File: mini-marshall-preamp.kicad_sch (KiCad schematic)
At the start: 46 parts, among them J1 LO, J2 HI, J3 OUT, J4 6V3, J5 370V GND, J6 370V, J7 6V3 GND, J8 6V3, J9 6V3 GND, U1 6N2P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

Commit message: Nice layout
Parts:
- J1: footprint Connector_Wire:SolderWire-1sqmm_1x03_P7.8mm_D1.4mm_OD3.9mm -> Connector_Wire:SolderWire-1sqmm_1x04_P7.8mm_D1.4mm_OD3.9mm
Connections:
- net anode: now reaches C14.1, R13.1, R16.2, U2.1 (A)
- net heater: no longer names the net of J8.1 (Pin_1), U1.4 (H1)
- net heater: no longer J4.1 (Pin_1), U2.4 (H1)
- new net: J4.1 (Pin_1), U2.4 (H1)
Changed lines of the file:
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@@
 		)
 	)
-	(label "heater"
-		(at 194.31 151.13 0)
+	(label "anode"
+		(at 199.39 34.29 0)
 		(effects
 			(font
@@
 		)
 	)
-	(label "heater"
-		(at 101.6 151.13 0)
-		(fields_autoplaced yes)
-		(effects
-			(font
-				(size 1.27 1.27)
-			)
-			(justify left bottom)
-		)
-		(property "heater" ""
-			(at 101.6 152.4 0)
-			(effects
-				(font
-					(size 1.27 1.27)
-					(italic yes)
-				)
-				(justify left)
-			)
-		)
-	)
 	(symbol
 		(lib_id "Connector:Screw_Terminal_01x01")
@@
 			)
 		)
-		(property "Footprint" "Connector_Wire:SolderWire-1sqmm_1x03_P7.8mm_D1.4mm_OD3.9mm"
+		(property "Footprint" "Connector_Wire:SolderWire-1sqmm_1x04_P7.8mm_D1.4mm_OD3.9mm"
 			(at 21.59 59.69 0)
 			(effects

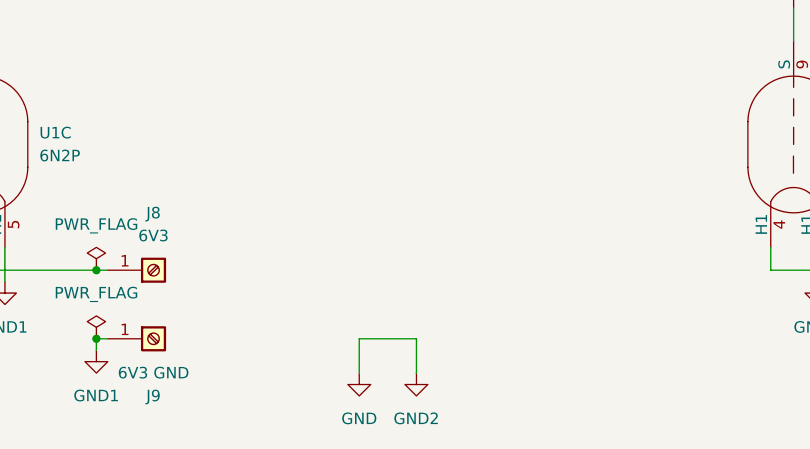
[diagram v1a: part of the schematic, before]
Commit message: Add mounting holes
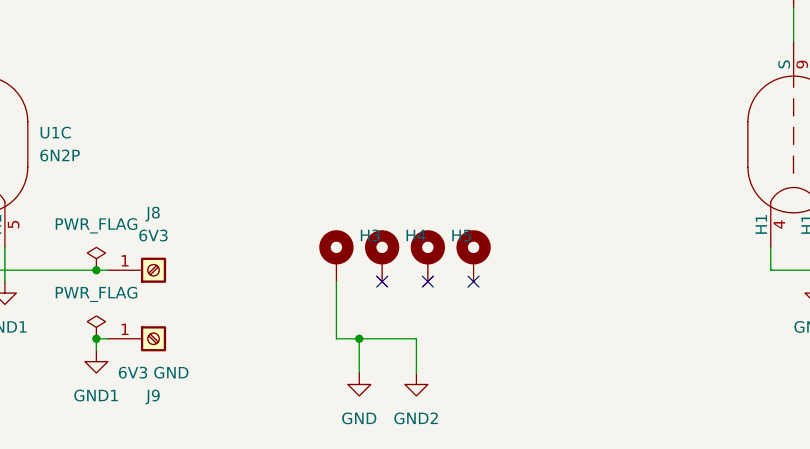
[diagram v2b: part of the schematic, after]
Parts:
- added H3: MountingHole_Pad, MountingHole:MountingHole_3.2mm_M3_Pad, symbol Mechanical:MountingHole_Pad
- added H4, H5, H6: MountingHole_Pad, MountingHole:MountingHole_3.2mm_M3, symbol Mechanical:MountingHole_Pad
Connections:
- net GND: now also H3.1
- no-connect marks 0 -> 3

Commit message: Tune clearances
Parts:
- J4, J5, J6, J7, J8, J9: footprint Connector_Wire:SolderWire-1.5sqmm_1x01_D1.7mm_OD3.9mm -> Connector_Wire:SolderWire-1sqmm_1x01_D1.4mm_OD2.7mm
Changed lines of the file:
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@@
 			)
 		)
-		(property "Footprint" "Connector_Wire:SolderWire-1.5sqmm_1x01_D1.7mm_OD3.9mm"
+		(property "Footprint" "Connector_Wire:SolderWire-1sqmm_1x01_D1.4mm_OD2.7mm"
 			(at 246.38 43.18 0)
 			(effects
@@
 			)
 		)
-		(property "Footprint" "Connector_Wire:SolderWire-1.5sqmm_1x01_D1.7mm_OD3.9mm"
+		(property "Footprint" "Connector_Wire:SolderWire-1sqmm_1x01_D1.4mm_OD2.7mm"
 			(at 116.84 151.13 0)
 			(effects
@@
 			)
 		)
-		(property "Footprint" "Connector_Wire:SolderWire-1.5sqmm_1x01_D1.7mm_OD3.9mm"
+		(property "Footprint" "Connector_Wire:SolderWire-1sqmm_1x01_D1.4mm_OD2.7mm"
 			(at 218.44 151.13 0)
 			(effects
@@
 			)
 		)
-		(property "Footprint" "Connector_Wire:SolderWire-1.5sqmm_1x01_D1.7mm_OD3.9mm"
+		(property "Footprint" "Connector_Wire:SolderWire-1sqmm_1x01_D1.4mm_OD2.7mm"
 			(at 246.38 34.29 0)
 			(effects
@@
 			)
 		)
-		(property "Footprint" "Connector_Wire:SolderWire-1.5sqmm_1x01_D1.7mm_OD3.9mm"
+		(property "Footprint" "Connector_Wire:SolderWire-1sqmm_1x01_D1.4mm_OD2.7mm"
 			(at 116.84 158.75 0)
 			(effects
@@
 			)
 		)
-		(property "Footprint" "Connector_Wire:SolderWire-1.5sqmm_1x01_D1.7mm_OD3.9mm"
+		(property "Footprint" "Connector_Wire:SolderWire-1sqmm_1x01_D1.4mm_OD2.7mm"
 			(at 218.44 158.75 0)
 			(effects

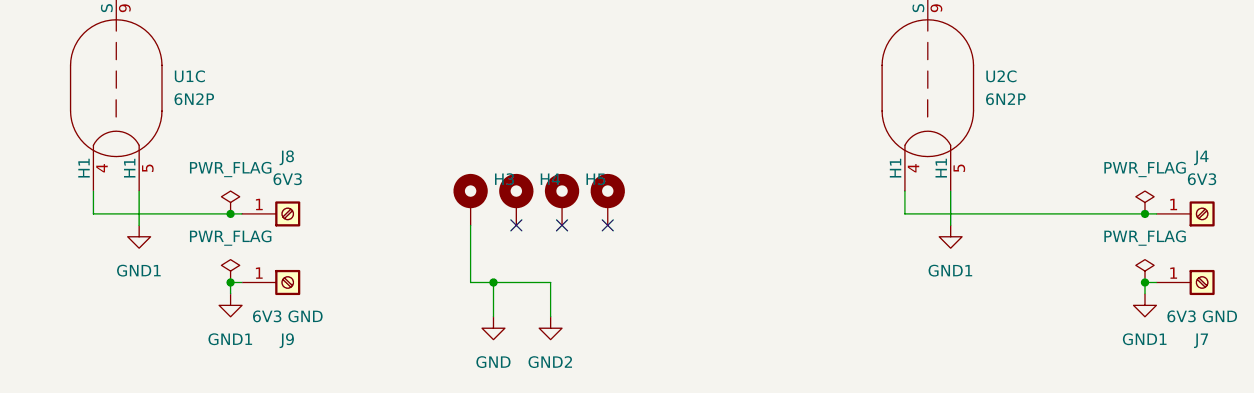
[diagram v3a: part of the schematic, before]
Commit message: Track widths and prettifying
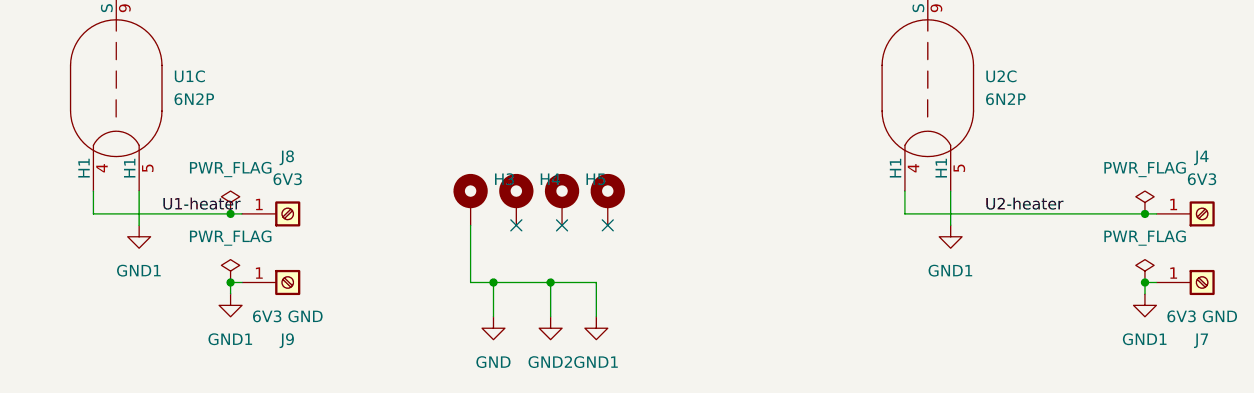
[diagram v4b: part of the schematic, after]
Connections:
- net GND1 is gone; now on net GND: J7.1 (Pin_1), J9.1 (Pin_1), U1.5 (H1), U2.5 (H1)
- net U1-heater: now reaches J8.1 (Pin_1), U1.4 (H1)
- net U2-heater: now reaches J4.1 (Pin_1), U2.4 (H1)
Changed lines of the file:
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@@
 	)
 	(junction
+		(at 146.05 158.75)
+		(diameter 0)
+		(color 0 0 0 0)
+	)
+	(junction
 		(at 121.92 34.29)
 		(diameter 0)
@@
 	(wire
 		(pts
+			(xy 151.13 162.56) (xy 151.13 158.75)
+		)
+		(stroke
+			(width 0)
+			(type default)
+		)
+	)
+	(wire
+		(pts
+			(xy 151.13 158.75) (xy 146.05 158.75)
+		)
+		(stroke
+			(width 0)
+			(type default)
+		)
+	)
+	(wire
+		(pts
 			(xy 142.24 71.12) (xy 142.24 74.93)
 		)
@@
 		)
 	)
+	(label "U2-heater"
+		(at 194.31 151.13 0)
+		(effects
+			(font
+				(size 1.27 1.27)
+			)
+			(justify left bottom)
+		)
+	)
+	(label "U1-heater"
+		(at 102.87 151.13 0)
+		(effects
+			(font
+				(size 1.27 1.27)
+			)
+			(justify left bottom)
+		)
+	)
 	(label "anode"
 		(at 199.39 34.29 0)
@@
 					(unit 1)
 				)
+			)
+		)
+	)
+	(symbol
+		(lib_id "power:GND1")
+		(at 151.13 162.56 0)
+		(unit 1)
+		(exclude_from_sim no)
+		(in_bom yes)
+		(on_board yes)
+		(dnp no)
+		(fields_autoplaced yes)
+		(property "Reference" "#PWR019"
+			(at 151.13 168.91 0)
+			(effects
+				(font
+					(size 1.27 1.27)
+				)
+				(hide yes)
+			)
+		)
+		(property "Value" "GND1"
+			(at 151.13 167.64 0)
+			(effects
+				(font
+					(size 1.27 1.27)
+				)
+			)
+		)
+		(property "Footprint" ""
+			(at 151.13 162.56 0)
+			(effects
+				(font
+					(size 1.27 1.27)
+				)
+				(hide yes)
+			)
+		)
+		(property "Datasheet" ""
+			(at 151.13 162.56 0)
+			(effects
+				(font
+					(size 1.27 1.27)
+				)
+				(hide yes)
+			)
+		)
+		(property "Description" "Power symbol creates a global label with name \"GND1\" , ground"
+			(at 151.13 162.56 0)
+			(effects
+				(font
+					(size 1.27 1.27)
+				)
+				(hide yes)
+			)
+		)
+		(pin "1"
+		)
+		(instances
+			(project "mini-marshall-preamp"
+				(path "/91d70738-8a39-4af9-b6d6-ee03b177697f"
+					(reference "#PWR019")
+					(unit 1)
+				)

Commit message: Upgrade to KiCad 10
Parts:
- C1, C14, C7: value 20u 450V -> 22u 450V
